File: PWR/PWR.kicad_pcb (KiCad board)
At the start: 2 copper layers, 74 x 72 mm, 20 parts, among them J1 +12v, SW1 SPDT

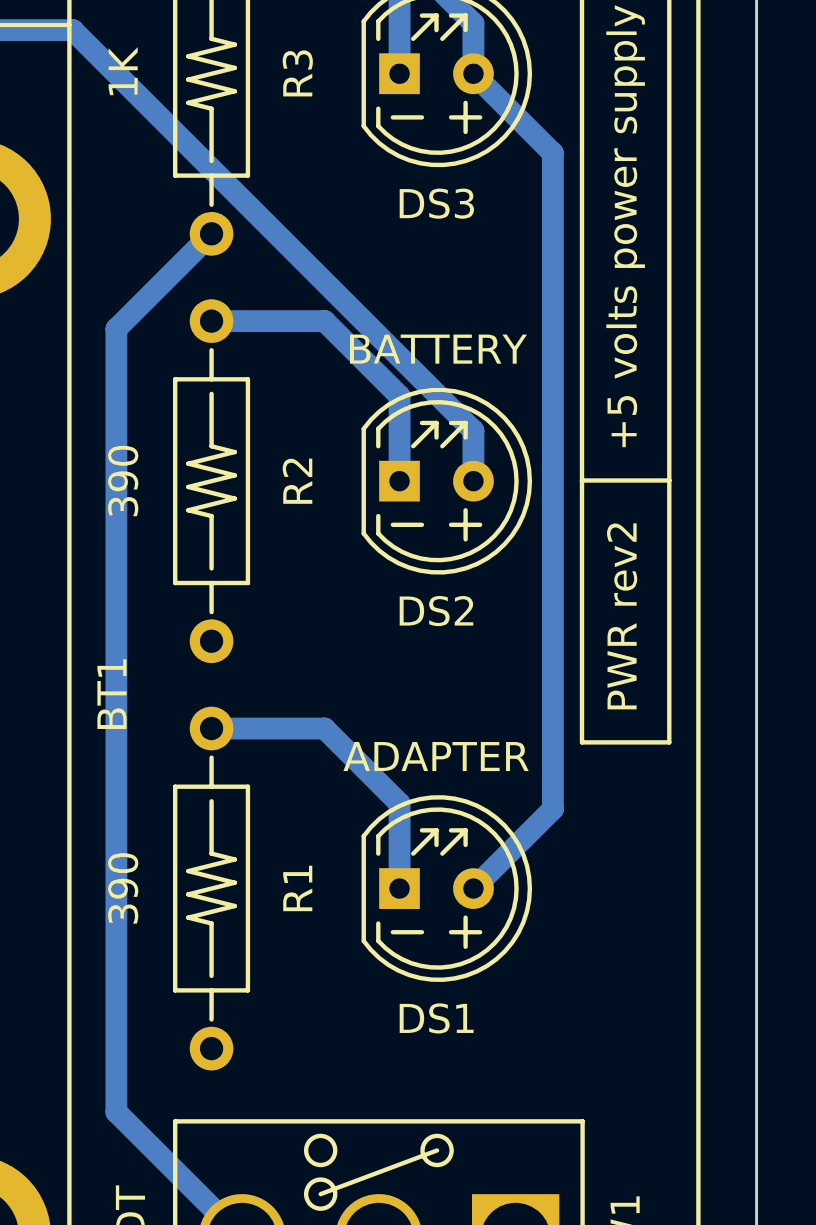
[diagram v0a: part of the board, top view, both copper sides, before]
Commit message: chore: Using D for LEDs instead of DS
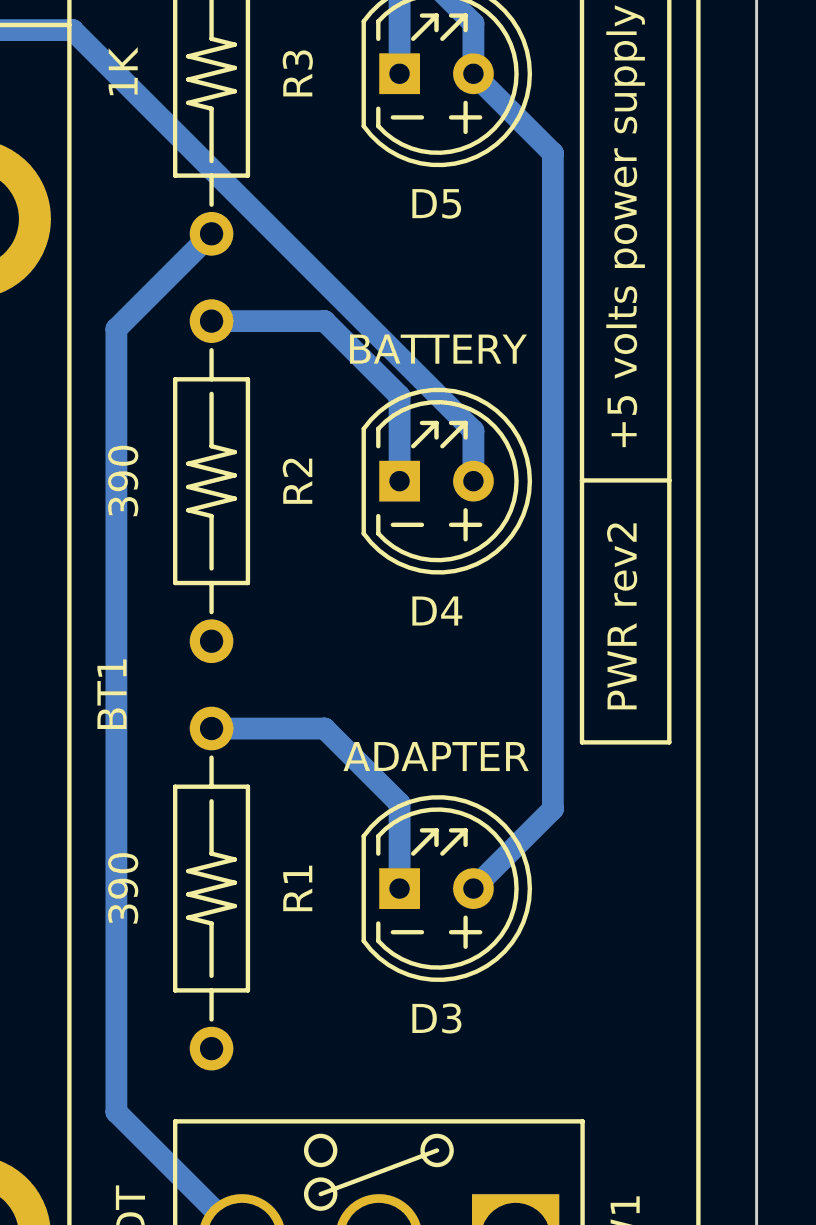
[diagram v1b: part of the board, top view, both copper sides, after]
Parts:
- renumbered DS1 to D3, DS2 to D4, DS3 to D5
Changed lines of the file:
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@@
   (net 5 "Net-(J2-Pin_1)")
   (net 6 "Net-(D1-A)")
-  (net 7 "Net-(DS1-K)")
-  (net 8 "Net-(DS2-K)")
-  (net 9 "Net-(DS3-K)")
+  (net 7 "Net-(D3-K)")
+  (net 8 "Net-(D4-K)")
+  (net 9 "Net-(D5-K)")
   (net 10 "Net-(SW1-B)")
   (net 11 "Net-(SW1-C)")
@@
       (stroke (width 0.15) (type solid)) (layer "F.SilkS"))
     (pad "1" thru_hole circle (at -5.5 0 270) (size 1.5 1.5) (drill 0.8) (layers "*.Cu" "*.Mask")
-      (net 7 "Net-(DS1-K)") (pintype "passive"))
+      (net 7 "Net-(D3-K)") (pintype "passive"))
     (pad "2" thru_hole circle (at 5.5 0 270) (size 1.5 1.5) (drill 0.8) (layers "*.Cu" "*.Mask")
       (net 4 "GND") (pintype "passive"))
@@
       (stroke (width 0.15) (type solid)) (layer "F.SilkS"))
     (pad "1" thru_hole circle (at -5.5 0 270) (size 1.5 1.5) (drill 0.8) (layers "*.Cu" "*.Mask")
-      (net 8 "Net-(DS2-K)") (pintype "passive"))
+      (net 8 "Net-(D4-K)") (pintype "passive"))
     (pad "2" thru_hole circle (at 5.5 0 270) (size 1.5 1.5) (drill 0.8) (layers "*.Cu" "*.Mask")
       (net 4 "GND") (pintype "passive"))
@@
     (property "ki_keywords" "LED diode")
     (attr through_hole)
-    (fp_text reference "DS3" (at 0 4.5) (layer "F.SilkS")
+    (fp_text reference "D5" (at 0 4.5) (layer "F.SilkS")
         (effects (font (size 1 1) (thickness 0.15)))
     )
@@
       (stroke (width 0.15) (type solid)) (layer "F.SilkS"))
     (pad "1" thru_hole rect (at -1.27 0) (size 1.4 1.4) (drill 0.7) (layers "*.Cu" "*.Mask")
-      (net 9 "Net-(DS3-K)") (pinfunction "K") (pintype "passive"))
+      (net 9 "Net-(D5-K)") (pinfunction "K") (pintype "passive"))
     (pad "2" thru_hole circle (at 1.27 0) (size 1.4 1.4) (drill 0.7) (layers "*.Cu" "*.Mask")
       (net 6 "Net-(D1-A)") (pinfunction "A") (pintype "passive"))
@@
       (net 11 "Net-(SW1-C)") (pintype "passive"))
     (pad "2" thru_hole circle (at 5.5 0 90) (size 1.5 1.5) (drill 0.8) (layers "*.Cu" "*.Mask")
-      (net 9 "Net-(DS3-K)") (pintype "passive"))
+      (net 9 "Net-(D5-K)") (pintype "passive"))
     (model "Resistor-Ohmite-OD-Series.step"
       (offset (xyz 0 0 0))
@@
     (property "ki_keywords" "LED diode")
     (attr through_hole)
-    (fp_text reference "DS2" (at 0 4.5) (layer "F.SilkS")
+    (fp_text reference "D4" (at 0 4.5) (layer "F.SilkS")
         (effects (font (size 1 1) (thickness 0.15)))
     )
@@
       (stroke (width 0.15) (type solid)) (layer "F.SilkS"))
     (pad "1" thru_hole rect (at -1.27 0) (size 1.4 1.4) (drill 0.7) (layers "*.Cu" "*.Mask")
-      (net 8 "Net-(DS2-K)") (pinfunction "K") (pintype "passive"))
+      (net 8 "Net-(D4-K)") (pinfunction "K") (pintype "passive"))
     (pad "2" thru_hole circle (at 1.27 0) (size 1.4 1.4) (drill 0.7) (layers "*.Cu" "*.Mask")
       (net 1 "Net-(BT1-+)") (pinfunction "A") (pintype "passive"))
@@
     (property "ki_keywords" "LED diode")
     (attr through_hole)
-    (fp_text reference "DS1" (at 0 4.5) (layer "F.SilkS")
+    (fp_text reference "D3" (at 0 4.5) (layer "F.SilkS")
         (effects (font (size 1 1) (thickness 0.15)))
     )
@@
       (stroke (width 0.15) (type solid)) (layer "F.SilkS"))
     (pad "1" thru_hole rect (at -1.27 0) (size 1.4 1.4) (drill 0.7) (layers "*.Cu" "*.Mask")
-      (net 7 "Net-(DS1-K)") (pinfunction "K") (pintype "passive"))
+      (net 7 "Net-(D3-K)") (pinfunction "K") (pintype "passive"))
     (pad "2" thru_hole circle (at 1.27 0) (size 1.4 1.4) (drill 0.7) (layers "*.Cu" "*.Mask")
       (net 6 "Net-(D1-A)") (pinfunction "A") (pintype "passive"))

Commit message: chore: Updated footprints and PCB
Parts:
- C1: footprint XS:Capacitor-Vishay-515D-8x11.5x3.5mm -> XS:Capacitor-Vishay-142-RHS-6.3x11x2.5mm
- C4: footprint XS:Capacitor-Vishay-515D-5x11x2mm -> XS:Capacitor-Vishay-142-RHS-5x11x2mm
- R1, R2, R3: footprint XS:Resistor-Ohmite-OD-Series -> XS:Resistor-Vishay-CCF07
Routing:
- net Net-(SW1-B): track 92.1 -> 104.9 mm
- net Net-(D4-K): track 10.5 -> 8.74 mm
- net Net-(D3-K): track 10.5 -> 8.74 mm
- net Net-(D1-A): track 102.8 -> 104.2 mm
- net Net-(BT1-+): track 74.7 -> 75.8 mm
- net Net-(BT1--): track 19.0 -> 18.1 mm
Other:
- board text added: "ON / OFF"
- board text removed: "OFF / ON"

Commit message: chore: Footprints update
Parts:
- D3, D4, D5: footprint XS:LED-T1-34-5mm -> XS:LED-T1-34-5mm-tabs
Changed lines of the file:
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@@
+        (effects (font (size 1 1) (thickness 0.15)))
+    )
+    (fp_text user "3" (at 3 2) (layer "F.SilkS")
         (effects (font (size 1 1) (thickness 0.15)))
     )
     (fp_text user "1" (at 6 -2.5) (layer "F.SilkS")
-        (effects (font (size 1 1) (thickness 0.15)))
-    )
-    (fp_text user "3" (at 3 2) (layer "F.SilkS")
         (effects (font (size 1 1) (thickness 0.15)))
     )
@@
       )
       (stroke (width 0) (type solid)) (fill solid) (layer "F.SilkS"))
-    (group "" (id 789e1d5d-7201-4f64-a4da-15dd6eb20434)
+    (group "" (id 4347b1de-c20c-44a7-b8a5-bebbe6f852bf)
       (members
-        fab436ef-3c09-4935-b604-11becdefbdea
+        611d2068-a1f4-43df-892e-be90d18f6539
       )
     )
@@
       )
       (stroke (width 0) (type solid)) (fill solid) (layer "F.SilkS"))
-    (group "" (id 8459da44-68fa-44e6-8d41-7ff0607a5b18)
+    (group "" (id 175c8e66-2f8f-4f32-9dbf-55b3d04578e9)
       (members
-        f0d22e53-f0c1-41d1-a55e-5456decd6a87
+        e95bf72a-a96e-4d1b-9e50-aba1f12c8120
       )
     )
@@
     )
   )
-  (footprint "XS:LED-T1-34-5mm" (layer "F.Cu")
+  (footprint "XS:LED-T1-34-5mm-tabs" (layer "F.Cu")
     (at 174 80)
     (property "Sheetfile" "PWR.kicad_sch")
@@
     (fp_line (start -2 1.2) (end -2 1.8)
       (stroke (width 0.15) (type solid)) (layer "F.SilkS"))
-    (fp_line (start -1.5 1.5) (end -0.5 1.5)
+    (fp_line (start -1.25 1.75) (end -0.25 1.75)
       (stroke (width 0.15) (type solid)) (layer "F.SilkS"))
     (fp_line (start -0.8 -1.2) (end 0 -2)
@@
     (fp_line (start 0 -2) (end 0 -1.5)
       (stroke (width 0.15) (type solid)) (layer "F.SilkS"))
+    (fp_line (start 0.25 1.75) (end 1.25 1.75)
+      (stroke (width 0.15) (type solid)) (layer "F.SilkS"))
     (fp_line (start 0.5 -2) (end 1 -2)
       (stroke (width 0.15) (type solid)) (layer "F.SilkS"))
-    (fp_line (start 0.5 1.5) (end 1.5 1.5)
+    (fp_line (start 0.75 2.25) (end 0.75 1.25)
       (stroke (width 0.15) (type solid)) (layer "F.SilkS"))
     (fp_line (start 1 -2) (end 0.2 -1.2)
@@
     (fp_line (start 1 -2) (end 1 -1.5)
       (stroke (width 0.15) (type solid)) (layer "F.SilkS"))
-    (fp_line (start 1 2) (end 1 1)
-      (stroke (width 0.15) (type solid)) (layer "F.SilkS"))
     (fp_arc (start -2.5 -1.8) (mid 3.208866 0) (end -2.5 1.8)
       (stroke (width 0.15) (type solid)) (layer "F.SilkS"))
     (fp_arc (start -2 -1.8) (mid 2.751019 0) (end -2 1.8)
       (stroke (width 0.15) (type solid)) (layer "F.SilkS"))
-    (pad "1" thru_hole rect (at -1.27 0) (size 1.4 1.4) (drill 0.7) (layers "*.Cu" "*.Mask")
+    (pad "1" thru_hole rect (at -1.27 0) (size 2 2) (drill 1.4) (layers "*.Cu" "*.Mask")
       (net 9 "Net-(D5-K)") (pinfunction "K") (pintype "passive"))
-    (pad "2" thru_hole circle (at 1.27 0) (size 1.4 1.4) (drill 0.7) (layers "*.Cu" "*.Mask")
+    (pad "2" thru_hole circle (at 1.27 0) (size 2 2) (drill 1.4) (layers "*.Cu" "*.Mask")
       (net 6 "Net-(D1-A)") (pinfunction "A") (pintype "passive"))
-    (model "LED-T1-34-5mm.step"
+    (model "LED-T1-34-5mm-tabs.step"
       (offset (xyz 0 0 0))
       (scale (xyz 1 1 1))
@@
     )
   )
-  (footprint "XS:LED-T1-34-5mm" (layer "F.Cu")
+  (footprint "XS:LED-T1-34-5mm-tabs" (layer "F.Cu")
     (at 174 94)
     (property "Sheetfile" "PWR.kicad_sch")
@@
     (fp_line (start -2 1.2) (end -2 1.8)
       (stroke (width 0.15) (type solid)) (layer "F.SilkS"))
-    (fp_line (start -1.5 1.5) (end -0.5 1.5)
+    (fp_line (start -1.25 1.75) (end -0.25 1.75)
       (stroke (width 0.15) (type solid)) (layer "F.SilkS"))
     (fp_line (start -0.8 -1.2) (end 0 -2)
@@
     (fp_line (start 0 -2) (end 0 -1.5)
       (stroke (width 0.15) (type solid)) (layer "F.SilkS"))
+    (fp_line (start 0.25 1.75) (end 1.25 1.75)
+      (stroke (width 0.15) (type solid)) (layer "F.SilkS"))
     (fp_line (start 0.5 -2) (end 1 -2)
       (stroke (width 0.15) (type solid)) (layer "F.SilkS"))
-    (fp_line (start 0.5 1.5) (end 1.5 1.5)
+    (fp_line (start 0.75 2.25) (end 0.75 1.25)
       (stroke (width 0.15) (type solid)) (layer "F.SilkS"))
     (fp_line (start 1 -2) (end 0.2 -1.2)
@@
     (fp_line (start 1 -2) (end 1 -1.5)
       (stroke (width 0.15) (type solid)) (layer "F.SilkS"))
-    (fp_line (start 1 2) (end 1 1)
-      (stroke (width 0.15) (type solid)) (layer "F.SilkS"))
     (fp_arc (start -2.5 -1.8) (mid 3.208866 0) (end -2.5 1.8)
       (stroke (width 0.15) (type solid)) (layer "F.SilkS"))
     (fp_arc (start -2 -1.8) (mid 2.751019 0) (end -2 1.8)
       (stroke (width 0.15) (type solid)) (layer "F.SilkS"))
-    (pad "1" thru_hole rect (at -1.27 0) (size 1.4 1.4) (drill 0.7) (layers "*.Cu" "*.Mask")
+    (pad "1" thru_hole rect (at -1.27 0) (size 2 2) (drill 1.4) (layers "*.Cu" "*.Mask")
       (net 8 "Net-(D4-K)") (pinfunction "K") (pintype "passive"))
-    (pad "2" thru_hole circle (at 1.27 0) (size 1.4 1.4) (drill 0.7) (layers "*.Cu" "*.Mask")
+    (pad "2" thru_hole circle (at 1.27 0) (size 2 2) (drill 1.4) (layers "*.Cu" "*.Mask")
       (net 1 "Net-(BT1-+)") (pinfunction "A") (pintype "passive"))
-    (model "LED-T1-34-5mm.step"
+    (model "LED-T1-34-5mm-tabs.step"
       (offset (xyz 0 0 0))
       (scale (xyz 1 1 1))
@@
     )
   )
-  (footprint "XS:LED-T1-34-5mm" (layer "F.Cu")
+  (footprint "XS:LED-T1-34-5mm-tabs" (layer "F.Cu")
     (at 174 108)
     (property "Sheetfile" "PWR.kicad_sch")
@@
     (fp_line (start -2 1.2) (end -2 1.8)
       (stroke (width 0.15) (type solid)) (layer "F.SilkS"))
-    (fp_line (start -1.5 1.5) (end -0.5 1.5)
+    (fp_line (start -1.25 1.75) (end -0.25 1.75)
       (stroke (width 0.15) (type solid)) (layer "F.SilkS"))
     (fp_line (start -0.8 -1.2) (end 0 -2)
@@
     (fp_line (start 0 -2) (end 0 -1.5)
       (stroke (width 0.15) (type solid)) (layer "F.SilkS"))
+    (fp_line (start 0.25 1.75) (end 1.25 1.75)
+      (stroke (width 0.15) (type solid)) (layer "F.SilkS"))
     (fp_line (start 0.5 -2) (end 1 -2)
       (stroke (width 0.15) (type solid)) (layer "F.SilkS"))
-    (fp_line (start 0.5 1.5) (end 1.5 1.5)
+    (fp_line (start 0.75 2.25) (end 0.75 1.25)
       (stroke (width 0.15) (type solid)) (layer "F.SilkS"))
     (fp_line (start 1 -2) (end 0.2 -1.2)
@@
     (fp_line (start 1 -2) (end 1 -1.5)
       (stroke (width 0.15) (type solid)) (layer "F.SilkS"))
-    (fp_line (start 1 2) (end 1 1)
-      (stroke (width 0.15) (type solid)) (layer "F.SilkS"))
     (fp_arc (start -2.5 -1.8) (mid 3.208866 0) (end -2.5 1.8)
       (stroke (width 0.15) (type solid)) (layer "F.SilkS"))
     (fp_arc (start -2 -1.8) (mid 2.751019 0) (end -2 1.8)
       (stroke (width 0.15) (type solid)) (layer "F.SilkS"))
-    (pad "1" thru_hole rect (at -1.27 0) (size 1.4 1.4) (drill 0.7) (layers "*.Cu" "*.Mask")
+    (pad "1" thru_hole rect (at -1.27 0) (size 2 2) (drill 1.4) (layers "*.Cu" "*.Mask")
       (net 7 "Net-(D3-K)") (pinfunction "K") (pintype "passive"))
-    (pad "2" thru_hole circle (at 1.27 0) (size 1.4 1.4) (drill 0.7) (layers "*.Cu" "*.Mask")
+    (pad "2" thru_hole circle (at 1.27 0) (size 2 2) (drill 1.4) (layers "*.Cu" "*.Mask")
       (net 6 "Net-(D1-A)") (pinfunction "A") (pintype "passive"))
-    (model "LED-T1-34-5mm.step"
+    (model "LED-T1-34-5mm-tabs.step"
       (offset (xyz 0 0 0))
       (scale (xyz 1 1 1))
